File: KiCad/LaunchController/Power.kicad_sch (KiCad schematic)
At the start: 38 parts, among them J1 DC_IN, J8 CONN_CONVERTER, Q1 TJ8S06M3L, Q2 2SC3325-Y, Q3 TJ8S06M3L, U3 INA219BIDCNT, U5 INA219BIDCNT

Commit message: 電圧から抵抗値を修正
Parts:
- R29: value 1kR -> 10kR
- TH1: value 1kR -> 10kR; footprint (none) -> Resistor_SMD:R_0603_1608Metric_Pad0.98x0.95mm_HandSolder
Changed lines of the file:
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@@
       (effects (font (size 1.27 1.27)) (justify right))
     )
-    (property "Value" "1kR" (at 327.66 42.545 0)
+    (property "Value" "10kR" (at 327.66 42.545 0)
       (effects (font (size 1.27 1.27)) (justify right))
     )
@@
       (effects (font (size 1.27 1.27)) (justify left))
     )
-    (property "Value" "1kR" (at 327.66 31.4325 0)
+    (property "Value" "10kR" (at 327.66 31.4325 0)
       (effects (font (size 1.27 1.27)) (justify left))
     )
-    (property "Footprint" "" (at 325.12 27.94 0)
+    (property "Footprint" "Resistor_SMD:R_0603_1608Metric_Pad0.98x0.95mm_HandSolder" (at 325.12 27.94 0)
       (effects (font (size 1.27 1.27)) hide)
     )
-    (property "Datasheet" "~" (at 325.12 27.94 0)
+    (property "Datasheet" "https://akizukidenshi.com/catalog/g/gP-05252/" (at 325.12 27.94 0)
       (effects (font (size 1.27 1.27)) hide)
     )

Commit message: さらに分割
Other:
- moved on the sheet: R11, R12, R16, R17, R29, TH1

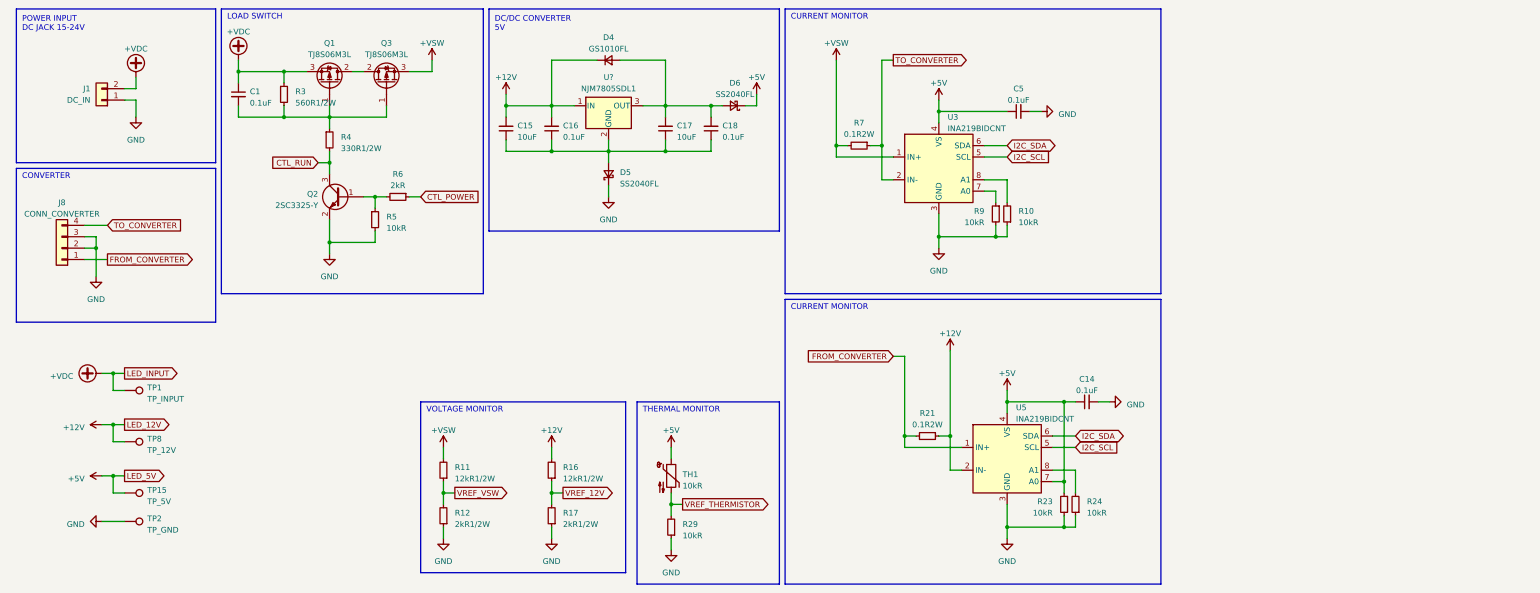
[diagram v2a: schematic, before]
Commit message: 端子台を選定
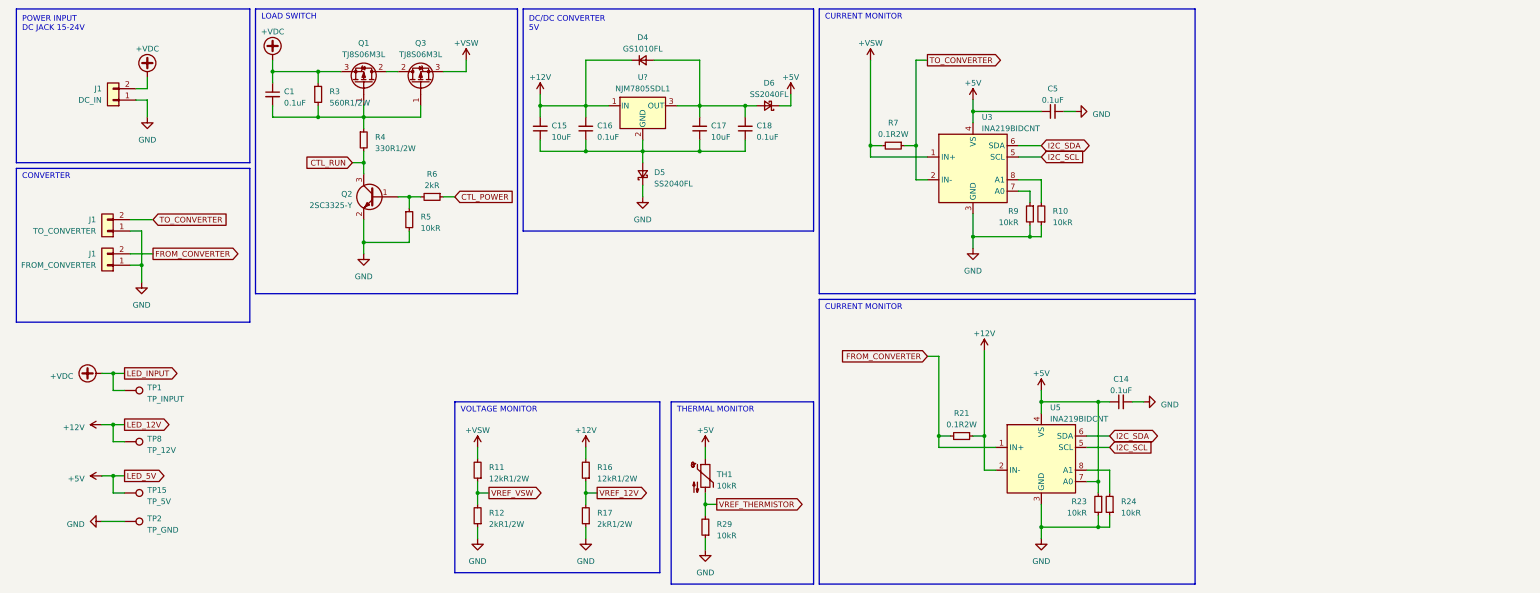
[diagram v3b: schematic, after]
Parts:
- removed J8: CONN_CONVERTER, Connector_JST:JST_XH_B4B-XH-A_1x04_P2.50mm_Vertical, symbol Connector_Generic:Conn_01x04
- added J1: TO_CONVERTER, TSRP_TerminalBlock_Alphaplus:TB411-2-2-E-1, symbol Connector_Generic:Conn_01x02
- added J1: FROM_CONVERTER, TSRP_TerminalBlock_Alphaplus:TB411-2-2-E-1, symbol Connector_Generic:Conn_01x02
- J1: footprint Connector_JST:JST_XH_B2B-XH-A_1x02_P2.50mm_Vertical -> TSRP_TerminalBlock_Alphaplus:TB411-2-2-E-1
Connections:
- net FROM_CONVERTER: now also J1.2 (Pin_2)
- net GND: now also J1.1 (Pin_1), J1.1 (Pin_1)
- net TO_CONVERTER: now also J1.2 (Pin_2)
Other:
- moved on the sheet: C1, C14, C15, C16, C17, C18, C5, D4, D5, D6, J1, Q1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

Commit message: 配線終わらん
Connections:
- net CTL_RUN renamed SW_RUN
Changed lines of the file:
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@@
-    )
-  )
-  (global_label "CTL_RUN" (shape input) (at 87.63 46.99 180) (fields_autoplaced)
-    (effects (font (size 1.27 1.27)) (justify right))
-    (property "Intersheetrefs" "${INTERSHEET_REFS}" (at 76.5599 46.99 0)
-      (effects (font (size 1.27 1.27)) (justify right) hide)
     )
   )
@@
     )
   )
+  (global_label "SW_RUN" (shape input) (at 87.63 46.99 180) (fields_autoplaced)
+    (effects (font (size 1.27 1.27)) (justify right))
+    (property "Intersheetrefs" "${INTERSHEET_REFS}" (at 77.1647 46.99 0)
+      (effects (font (size 1.27 1.27)) (justify right) hide)
+    )
+  )

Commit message: 電源周りできた
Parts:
- R11, R16: value 12kR1/2W -> 12kR
- R12, R17: value 2kR1/2W -> 2kR
- R3: value 560R1/2W -> 5.6R; footprint Resistor_SMD:R_1206_3216Metric_Pad1.30x1.75mm_HandSolder -> Resistor_SMD:R_0603_1608Metric_Pad0.98x0.95mm_HandSolder
- R4: value 330R1/2W -> 3.3R; footprint Resistor_SMD:R_1206_3216Metric_Pad1.30x1.75mm_HandSolder -> Resistor_SMD:R_0603_1608Metric_Pad0.98x0.95mm_HandSolder
- R6: value 2kR -> 2.2kR

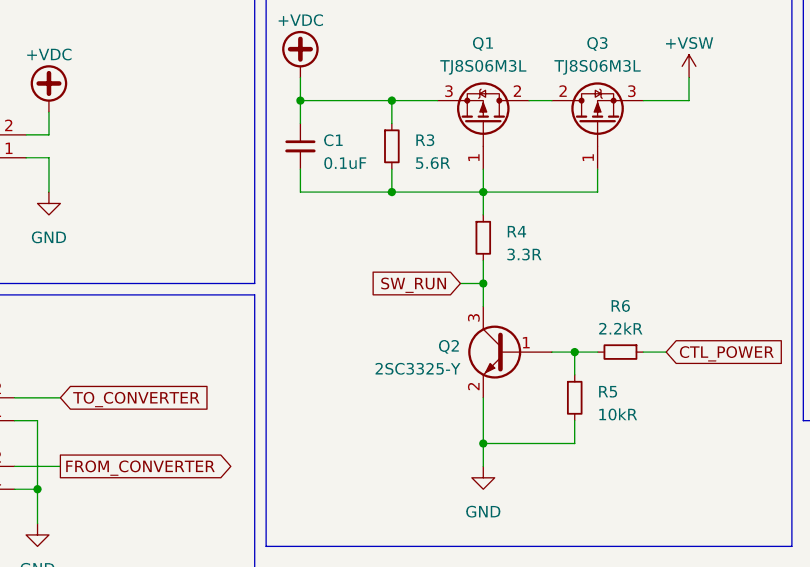
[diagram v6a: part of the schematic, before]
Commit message: あとはDRC解決とビア打ち
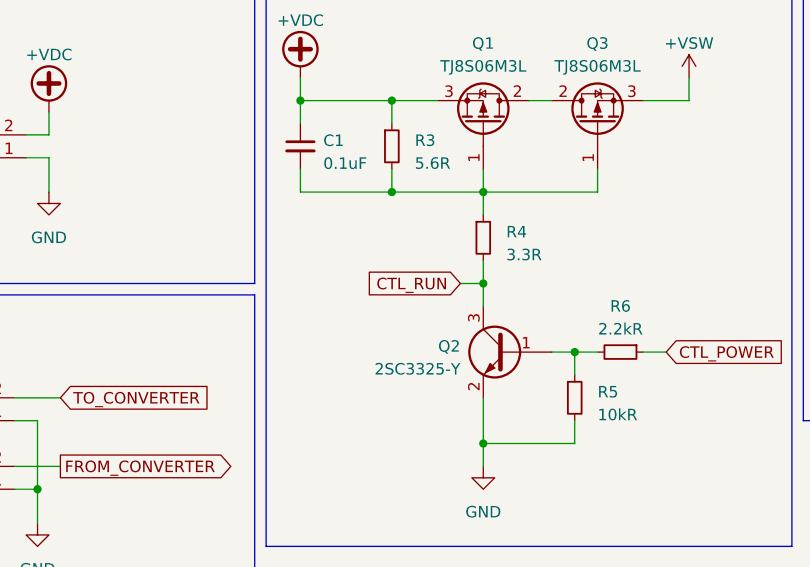
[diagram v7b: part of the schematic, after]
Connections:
- net SW_RUN renamed CTL_RUN
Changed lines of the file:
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@@
     )
   )
-  (global_label "SW_RUN" (shape input) (at 87.63 46.99 180) (fields_autoplaced)
+  (global_label "CTL_RUN" (shape input) (at 87.63 46.99 180) (fields_autoplaced)
     (effects (font (size 1.27 1.27)) (justify right))
-    (property "Intersheetrefs" "${INTERSHEET_REFS}" (at 77.1647 46.99 0)
+    (property "Intersheetrefs" "${INTERSHEET_REFS}" (at 76.5599 46.99 0)
       (effects (font (size 1.27 1.27)) (justify right) hide)
     )

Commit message: 選定部品を調整
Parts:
- C15, C17: footprint Capacitor_SMD:C_0603_1608Metric_Pad1.08x0.95mm_HandSolder -> Capacitor_SMD:C_1206_3216Metric_Pad1.33x1.80mm_HandSolder
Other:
- moved on the sheet: C14, C5, R10, R21, R23, R24, R7, R9, U3, U5
